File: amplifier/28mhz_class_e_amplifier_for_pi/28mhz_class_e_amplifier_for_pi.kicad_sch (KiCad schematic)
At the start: 20 parts, among them M1 RD16HHF1, U1 LT1818

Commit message: Switch to 50 ohm impedance
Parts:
- removed R5: 75, symbol ltspice:res
- added J1: Conn_Coaxial_Small, symbol Connector:Conn_Coaxial_Small
- added amp_matching1, matching_filter1, pre_main1: 0, symbol Device:R
- C10, C8: value 82p -> 130p; footprint Capacitor_SMD:C_0805_2012Metric -> (none)
- C7: value 130p -> 110p; footprint 0505:CAPC1514X130N -> (none)
- C9: value 150p -> 220p; footprint Capacitor_SMD:C_0805_2012Metric -> (none)
- L5: value 160n -> 140n; footprint Capacitor_SMD:C_0805_2012Metric -> (none)
- L6, L7: value 560n -> 390n; footprint 560nH:AISC-1008 -> (none)
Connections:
- net 0: now also J1.2 (Ext)
- net at C8.1, L6.2: now also matching_filter1.2; no longer C7.1
- net at R3.1, U1.3 (OUT): now also pre_main1.1; no longer M1.2 (G)
- net at L8.1, L9.1: now also amp_matching1.1; no longer C6.2
- net at C10.1, L7.1: now also J1.1 (In)
- new net: M1.2 (G), pre_main1.2
- new net: C6.2, amp_matching1.2
- new net: C7.1, matching_filter1.1

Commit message: current progress
footprints defined for everything except antenna and battery connectors
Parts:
- CF1: renamed from C8; value 130p -> 120p; footprint (none) -> Capacitor_SMD:C_0805_2012Metric
- CF2: renamed from C9; footprint (none) -> Capacitor_SMD:C_0805_2012Metric
- CF3: renamed from C10; value 130p -> 120p; footprint (none) -> Capacitor_SMD:C_0805_2012Metric
- CL1: renamed from C7; footprint (none) -> Capacitor_SMD:C_0805_2012Metric
- CS1: renamed from C6; value 190p -> 200p
- L2_a1: renamed from L8; value 1.8µ -> 1.5µ; footprint 1.8uH:LQH43MN470K03L -> Inductor_SMD:L_0805_2012Metric
- L2_b1: renamed from L9; value 470n -> 500n; footprint (none) -> wireinductor1:2929SQ501GEC
- LF1: renamed from L6; footprint (none) -> wireinductor0:2929SQ391GEC
- LF2: renamed from L7; footprint (none) -> wireinductor0:2929SQ391GEC
- LI1: renamed from L5; value 140n -> 130n; footprint (none) -> custom:130nH_WLQC2222H0GR13LB
- R0: renamed from pre_main1; footprint (none) -> Resistor_SMD:R_2512_6332Metric
- R1: renamed from amp_matching1; footprint (none) -> Resistor_SMD:R_2512_6332Metric
- R2: renamed from matching_filter1; footprint (none) -> Resistor_SMD:R_2512_6332Metric
- RF1: renamed from R3; footprint (none) -> 1Kohm:RESAD1625W54L665D240
- RI1: renamed from R1; footprint (none) -> 1Kohm:RESAD1625W54L665D240
- VBATTERY1: footprint (none) -> 1Kohm:RESAD1625W54L665D240
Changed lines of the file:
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@@
 		(on_board yes)
 		(dnp no)
-		(property "Reference" "C8"
+		(property "Reference" "CF1"
 			(at 231.775 109.855 0)
 			(effects
@@
 			)
 		)
-		(property "Value" "130p"
+		(property "Value" "120p"
 			(at 231.775 113.665 0)
 			(effects
@@
 			)
 		)
-		(property "Footprint" ""
+		(property "Footprint" "Capacitor_SMD:C_0805_2012Metric"
 			(at 229.87 109.22 0)
 			(effects
@@
 			(project ""
 				(path "/c76b4f53-cf38-425a-9e08-4e96ea8ec0d5"
-					(reference "C8")
+					(reference "CF1")
 					(unit 1)
 				)
@@
 		(on_board yes)
 		(dnp no)
-		(property "Reference" "L6"
+		(property "Reference" "LF1"
 			(at 236.855 103.2764 90)
 			(effects
@@
 			)
 		)
-		(property "Footprint" ""
+		(property "Footprint" "wireinductor0:2929SQ391GEC"
 			(at 241.3 102.87 0)
 			(effects
@@
 			(project ""
 				(path "/c76b4f53-cf38-425a-9e08-4e96ea8ec0d5"
-					(reference "L6")
+					(reference "LF1")
 					(unit 1)
 				)
@@
 		(on_board yes)
 		(dnp no)
-		(property "Reference" "R3"
+		(property "Reference" "RF1"
 			(at 88.1888 123.6726 90)
 			(effects
@@
 			)
 		)
-		(property "Footprint" ""
+		(property "Footprint" "1Kohm:RESAD1625W54L665D240"
 			(at 92.71 116.84 0)
 			(effects
@@
 			(project ""
 				(path "/c76b4f53-cf38-425a-9e08-4e96ea8ec0d5"
-					(reference "R3")
+					(reference "RF1")
 					(unit 1)
 				)
@@
 		(on_board yes)
 		(dnp no)
-		(property "Reference" "C6"
+		(property "Reference" "CS1"
 			(at 195.58 102.87 90)
 			(effects
@@
 			)
 		)
-		(property "Value" "190p"
+		(property "Value" "200p"
 			(at 195.58 105.41 90)
 			(effects
@@
 			(project ""
 				(path "/c76b4f53-cf38-425a-9e08-4e96ea8ec0d5"
-					(reference "C6")
+					(reference "CS1")
 					(unit 1)
 				)
@@
 		(on_board yes)
 		(dnp no)
-		(property "Reference" "L8"
+		(property "Reference" "L2_a1"
 			(at 161.925 99.4664 90)
 			(effects
@@
 			)
 		)
-		(property "Value" "1.8µ"
+		(property "Value" "1.5µ"
 			(at 161.925 101.6 90)
 			(effects
@@
 			)
 		)
-		(property "Footprint" "1.8uH:LQH43MN470K03L"
+		(property "Footprint" "Inductor_SMD:L_0805_2012Metric"
 			(at 166.37 99.06 0)
 			(effects
@@
 			(project ""
 				(path "/c76b4f53-cf38-425a-9e08-4e96ea8ec0d5"
-					(reference "L8")
+					(reference "L2_a1")
 					(unit 1)
 				)
@@
 		(on_board yes)
 		(dnp no)
-		(property "Reference" "C10"
+		(property "Reference" "CF3"
 			(at 262.255 109.855 0)
 			(effects
@@
 			)
 		)
-		(property "Value" "130p"
+		(property "Value" "120p"
 			(at 262.255 113.665 0)
 			(effects
@@
 			)
 		)
-		(property "Footprint" ""
+		(property "Footprint" "Capacitor_SMD:C_0805_2012Metric"
 			(at 260.35 109.22 0)
 			(effects
@@
 			(project ""
 				(path "/c76b4f53-cf38-425a-9e08-4e96ea8ec0d5"
-					(reference "C10")
+					(reference "CF3")
 					(unit 1)
 				)
@@
 			)
 		)
-		(property "Footprint" ""
+		(property "Footprint" "1Kohm:RESAD1625W54L665D240"
 			(at 106.68 93.98 0)
 			(effects
@@
 		(on_board yes)
 		(dnp no)
-		(property "Reference" "C7"
+		(property "Reference" "CL1"
 			(at 212.09 102.87 90)
 			(effects
@@
 			)
 		)
-		(property "Footprint" ""
+		(property "Footprint" "Capacitor_SMD:C_0805_2012Metric"
 			(at 214.63 102.87 0)
 			(effects
@@
 			(project ""
 				(path "/c76b4f53-cf38-425a-9e08-4e96ea8ec0d5"
-					(reference "C7")
+					(reference "CL1")
 					(unit 1)
 				)
@@
 		(on_board yes)
 		(dnp no)
-		(property "Reference" "L5"
+		(property "Reference" "LI1"
 			(at 204.8002 112.395 0)
 			(effects
@@
 			)
 		)
-		(property "Value" "140n"
+		(property "Value" "130n"
 			(at 204.8002 115.57 0)
 			(effects
@@
 			)
 		)
-		(property "Footprint" ""
+		(property "Footprint" "custom:130nH_WLQC2222H0GR13LB"
 			(at 201.93 109.22 0)
 			(effects
@@
 			(project ""
 				(path "/c76b4f53-cf38-425a-9e08-4e96ea8ec0d5"
-					(reference "L5")
+					(reference "LI1")
 					(unit 1)
 				)
@@
 		(on_board yes)
 		(dnp no)
-		(property "Reference" "L9"
+		(property "Reference" "L2_b1"
 			(at 161.925 107.0864 90)
 			(effects
@@
 			)
 		)
-		(property "Value" "470n"
+		(property "Value" "500n"
 			(at 161.925 109.22 90)
 			(effects
@@
 			)
 		)
-		(property "Footprint" ""
+		(property "Footprint" "wireinductor1:2929SQ501GEC"
 			(at 166.37 106.68 0)
 			(effects
@@
 			(project ""
 				(path "/c76b4f53-cf38-425a-9e08-4e96ea8ec0d5"
-					(reference "L9")
+					(reference "L2_b1")
 					(unit 1)
 				)
@@
 		(on_board yes)
 		(dnp no)
-		(property "Reference" "L7"
+		(property "Reference" "LF2"
 			(at 253.365 103.2764 90)
 			(effects
@@
 			)
 		)
-		(property "Footprint" ""
+		(property "Footprint" "wireinductor0:2929SQ391GEC"
 			(at 257.81 102.87 0)
 			(effects
@@
 			(project ""
 				(path "/c76b4f53-cf38-425a-9e08-4e96ea8ec0d5"
-					(reference "L7")
+					(reference "LF2")
 					(unit 1)
 				)
@@
 		(dnp no)
 		(fields_autoplaced yes)
-		(property "Reference" "amp_matching1"
+		(property "Reference" "R1"
 			(at 179.07 97.79 90)
 			(effects
@@
 			)
 		)
-		(property "Footprint" ""
+		(property "Footprint" "Resistor_SMD:R_2512_6332Metric"
 			(at 179.07 105.918 90)
 			(effects
@@
 			(project ""
 				(path "/c76b4f53-cf38-425a-9e08-4e96ea8ec0d5"
-					(reference "amp_matching1")
+					(reference "R1")
 					(unit 1)
 				)
@@
 		(on_board yes)
 		(dnp no)
-		(property "Reference" "R1"
+		(property "Reference" "RI1"
 			(at 77.8002 123.825 0)
 			(effects
@@
 			)
 		)
-		(property "Footprint" ""
+		(property "Footprint" "1Kohm:RESAD1625W54L665D240"
 			(at 74.93 120.65 0)
 			(effects
@@
 			(project ""
 				(path "/c76b4f53-cf38-425a-9e08-4e96ea8ec0d5"
-					(reference "R1")
+					(reference "RI1")
 					(unit 1)
 				)
@@
 				)
 				(justify bottom)
-				(hide yes)
 			)
 		)
@@
 				)
 				(justify top)
-				(hide yes)
 			)
 		)
@@
 		(dnp no)
 		(fields_autoplaced yes)
-		(property "Reference" "pre_main1"
+		(property "Reference" "R0"
 			(at 106.68 106.68 90)
 			(effects
@@
 			)
 		)
-		(property "Footprint" ""
+		(property "Footprint" "Resistor_SMD:R_2512_6332Metric"
 			(at 106.68 114.808 90)
 			(effects
@@
 			(project ""
 				(path "/c76b4f53-cf38-425a-9e08-4e96ea8ec0d5"
-					(reference "pre_main1")
+					(reference "R0")
 					(unit 1)
 				)
@@
 		(on_board yes)
 		(dnp no)
-		(property "Reference" "C9"
+		(property "Reference" "CF2"
 			(at 245.745 109.855 0)
 			(effects
@@
 			)
 		)
-		(property "Footprint" ""
+		(property "Footprint" "Capacitor_SMD:C_0805_2012Metric"
 			(at 243.84 109.22 0)
 			(effects
@@
 			(project ""
 				(path "/c76b4f53-cf38-425a-9e08-4e96ea8ec0d5"
-					(reference "C9")
+					(reference "CF2")
 					(unit 1)
 				)
@@
 		(dnp no)
 		(fields_autoplaced yes)
-		(property "Reference" "matching_filter1"
+		(property "Reference" "R2"
 			(at 223.52 97.79 90)
 			(effects
@@
 			)
 		)
-		(property "Footprint" ""
+		(property "Footprint" "Resistor_SMD:R_2512_6332Metric"
 			(at 223.52 105.918 90)
 			(effects
@@
 			(project "28mhz_class_e_amplifier_for_pi"
 				(path "/c76b4f53-cf38-425a-9e08-4e96ea8ec0d5"
-					(reference "matching_filter1")
-					(unit 1)
-				)
+					(reference "R2")
+					(unit 1)
+				)

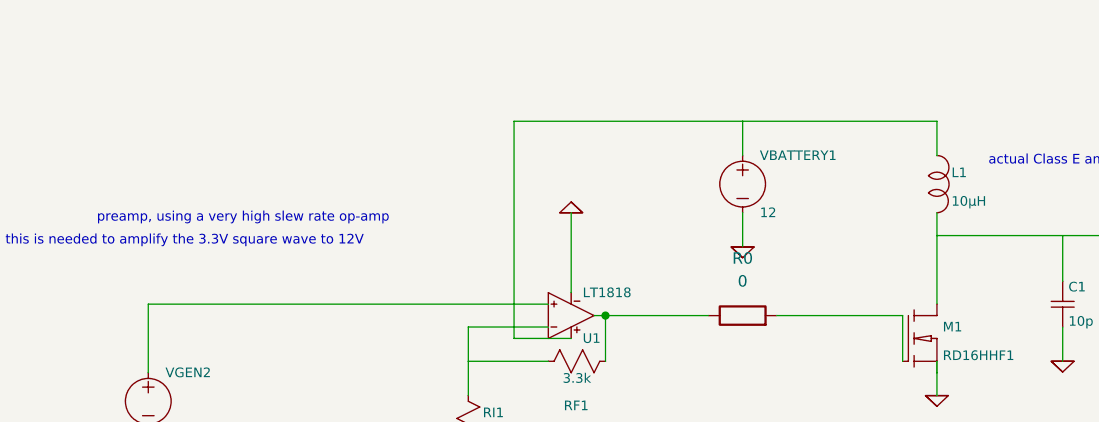
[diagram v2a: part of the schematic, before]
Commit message: ALL FOOTPRINTS ASSIGNED WE ARE COOKING
still need voltage regulator for Pi, it's ok :D
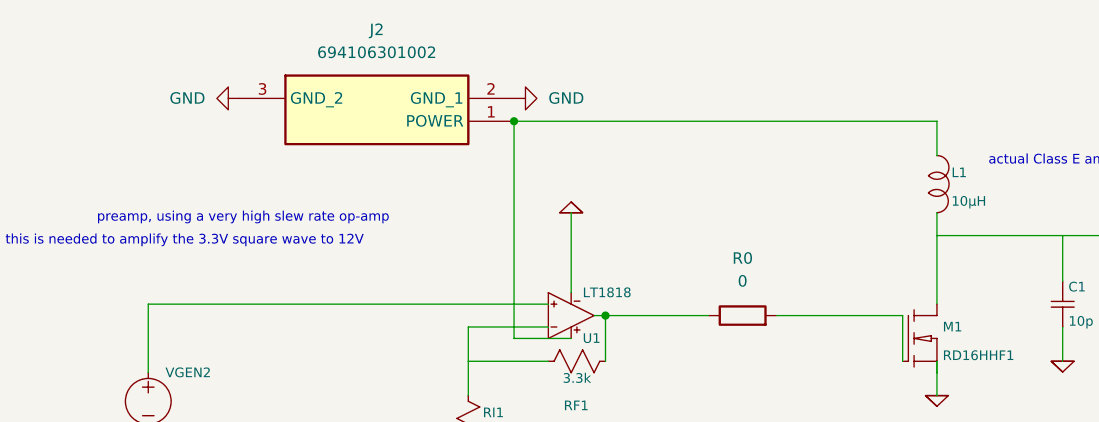
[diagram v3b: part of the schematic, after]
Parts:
- removed VBATTERY1: 12, 1Kohm:RESAD1625W54L665D240, symbol ltspice:voltage
- added J2: 694106301002, barreljack:694106301002_1, symbol barreljack:694106301002
- J1: footprint (none) -> BNC:CONBNC002
- VGEN2: footprint (none) -> Connector_PinHeader_2.54mm:PinHeader_1x02_P2.54mm_Vertical
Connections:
- net at L1.1, U1.4 (VCC): now also J2.1 (POWER)
- new net GND: J2.2 (GND_1), J2.3 (GND_2)
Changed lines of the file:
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@@
+		(color 0 0 0 0)
+	)
+	(junction
+		(at 81.28 91.44)
+		(diameter 0)
 		(color 0 0 0 0)
 	)
@@
 	(wire
 		(pts
-			(xy 106.68 105.41) (xy 106.68 101.6)
-		)
-		(stroke
-			(width 0.1524)
-			(type solid)
-		)
-	)
-	(wire
-		(pts
 			(xy 214.63 104.14) (xy 219.71 104.14)
 		)
@@
 	(wire
 		(pts
-			(xy 106.68 95.25) (xy 106.68 91.44)
-		)
-		(stroke
-			(width 0.1524)
-			(type solid)
-		)
-	)
-	(wire
-		(pts
 			(xy 245.11 109.22) (xy 245.11 104.14)
 		)
@@
 	(wire
 		(pts
-			(xy 128.27 91.44) (xy 106.68 91.44)
-		)
-		(stroke
-			(width 0.1524)
-			(type solid)
-		)
-	)
-	(wire
-		(pts
 			(xy 142.24 109.22) (xy 142.24 104.14)
 		)
@@
 	(wire
 		(pts
-			(xy 106.68 91.44) (xy 81.28 91.44)
+			(xy 81.28 91.44) (xy 128.27 91.44)
 		)
 		(stroke
@@
 				(path "/c76b4f53-cf38-425a-9e08-4e96ea8ec0d5"
 					(reference "CF3")
-					(unit 1)
-				)
-			)
-		)
-	)
-	(symbol
-		(lib_id "ltspice:voltage")
-		(at 106.68 93.98 0)
-		(unit 1)
-		(exclude_from_sim no)
-		(in_bom yes)
-		(on_board yes)
-		(dnp no)
-		(property "Reference" "VBATTERY1"
-			(at 108.585 95.25 0)
-			(effects
-				(font
-					(size 1.0668 1.0668)
-				)
-				(justify left)
-			)
-		)
-		(property "Value" "12"
-			(at 108.585 101.6 0)
-			(effects
-				(font
-					(size 1.0668 1.0668)
-				)
-				(justify left)
-			)
-		)
-		(property "Footprint" "1Kohm:RESAD1625W54L665D240"
-			(at 106.68 93.98 0)
-			(effects
-				(font
-					(size 1.27 1.27)
-				)
-				(hide yes)
-			)
-		)
-		(property "Datasheet" ""
-			(at 106.68 93.98 0)
-			(effects
-				(font
-					(size 1.27 1.27)
-				)
-				(hide yes)
-			)
-		)
-		(property "Description" ""
-			(at 106.68 93.98 0)
-			(effects
-				(font
-					(size 1.27 1.27)
-				)
-				(hide yes)
-			)
-		)
-		(property "Sim.Device" "SPICE"
-			(at 106.68 93.98 0)
-			(effects
-				(font
-					(size 1.27 1.27)
-				)
-				(hide yes)
-			)
-		)
-		(property "Sim.Params" "type=\"V\" model=\"${VALUE}\" "
-			(at 106.68 93.98 0)
-			(effects
-				(font
-					(size 1.0668 1.0668)
-				)
-				(justify left)
-				(hide yes)
-			)
-		)
-		(pin "1"
-		)
-		(pin "2"
-		)
-		(instances
-			(project ""
-				(path "/c76b4f53-cf38-425a-9e08-4e96ea8ec0d5"
-					(reference "VBATTERY1")
 					(unit 1)
 				)
@@
 			)
 		)
-		(property "Footprint" ""
+		(property "Footprint" "BNC:CONBNC002"
 			(at 273.05 110.49 0)
 			(effects
@@
 			)
 		)
-		(property "Footprint" ""
+		(property "Footprint" "Connector_PinHeader_2.54mm:PinHeader_1x02_P2.54mm_Vertical"
 			(at 40.64 118.11 0)
 			(effects
@@
 	)
 	(symbol
+		(lib_id "barreljack:694106301002")
+		(at 50.8 88.9 0)
+		(unit 1)
+		(exclude_from_sim no)
+		(in_bom yes)
+		(on_board yes)
+		(dnp no)
+		(fields_autoplaced yes)
+		(property "Reference" "J2"
+			(at 66.04 81.28 0)
+			(effects
+				(font
+					(size 1.27 1.27)
+				)
+			)
+		)
+		(property "Value" "694106301002"
+			(at 66.04 83.82 0)
+			(effects
+				(font
+					(size 1.27 1.27)
+				)
+			)
+		)
+		(property "Footprint" "barreljack:694106301002_1"
+			(at 77.47 183.82 0)
+			(effects
+				(font
+					(size 1.27 1.27)
+				)
+				(justify left top)
+				(hide yes)
+			)
+		)
+		(property "Datasheet" "https://datasheet.datasheetarchive.com/originals/distributors/Datasheets_SAMA/1c153bd2ba42bb51bda59ee4cd9765cd.pdf"
+			(at 77.47 283.82 0)
+			(effects
+				(font
+					(size 1.27 1.27)
+				)
+				(justify left top)
+				(hide yes)
+			)
+		)
+		(property "Description" "WURTH ELEKTRONIK - 694106301002 - CONNECTOR, POWER ENTRY, JACK, 3A, 20VDC"
+			(at 50.8 88.9 0)
+			(effects
+				(font
+					(size 1.27 1.27)
+				)
+				(hide yes)
+			)
+		)
+		(property "Height" ""
+			(at 77.47 483.82 0)
+			(effects
+				(font
+					(size 1.27 1.27)
+				)
+				(justify left top)
+				(hide yes)
+			)
+		)
+		(property "Mouser Part Number" "710-694106301002"
+			(at 77.47 583.82 0)
+			(effects
+				(font
+					(size 1.27 1.27)
+				)
+				(justify left top)
+				(hide yes)
+			)
+		)
+		(property "Mouser Price/Stock" "https://www.mouser.co.uk/ProductDetail/Wurth-Elektronik/694106301002?qs=a9WhcLg8qCwOEkcI62k5mA%3D%3D"
+			(at 77.47 683.82 0)
+			(effects
+				(font
+					(size 1.27 1.27)
+				)
+				(justify left top)
+				(hide yes)
+			)
+		)
+		(property "Manufacturer_Name" "Wurth Elektronik"
+			(at 77.47 783.82 0)
+			(effects
+				(font
+					(size 1.27 1.27)
+				)
+				(justify left top)
+				(hide yes)
+			)
+		)
+		(property "Manufacturer_Part_Number" "694106301002"
+			(at 77.47 883.82 0)
+			(effects
+				(font
+					(size 1.27 1.27)
+				)
+				(justify left top)
+				(hide yes)
+			)
+		)
+		(pin "3"
+		)
+		(pin "2"
+		)
+		(pin "1"
+		)
+		(instances
+			(project ""
+				(path "/c76b4f53-cf38-425a-9e08-4e96ea8ec0d5"
+					(reference "J2")
+					(unit 1)
+				)
+			)
+		)
+	)
+	(symbol
 		(lib_id "ltspice:cap")
 		(at 153.67 102.87 270)
@@
 				(path "/c76b4f53-cf38-425a-9e08-4e96ea8ec0d5"
 					(reference "#GND03")
+					(unit 1)
+				)
+			)
+		)
+	)
+	(symbol
+		(lib_id "power:GND")
+		(at 81.28 88.9 90)
+		(unit 1)
+		(exclude_from_sim no)
+		(in_bom yes)
+		(on_board yes)
+		(dnp no)
+		(fields_autoplaced yes)
+		(property "Reference" "#PWR01"
+			(at 87.63 88.9 0)
+			(effects
+				(font
+					(size 1.27 1.27)
+				)
+				(hide yes)
+			)
+		)
+		(property "Value" "GND"
+			(at 85.09 88.8999 90)
+			(effects
+				(font
+					(size 1.27 1.27)
+				)
+				(justify right)
+			)
+		)
+		(property "Footprint" ""
+			(at 81.28 88.9 0)
+			(effects
+				(font
+					(size 1.27 1.27)
+				)
+				(hide yes)
+			)
+		)
+		(property "Datasheet" ""
+			(at 81.28 88.9 0)
+			(effects
+				(font
+					(size 1.27 1.27)
+				)
+				(hide yes)
+			)
+		)
+		(property "Description" "Power symbol creates a global label with name \"GND\" , ground"
+			(at 81.28 88.9 0)
+			(effects
+				(font
+					(size 1.27 1.27)
+				)
+				(hide yes)
+			)
+		)
+		(pin "1"
+		)
+		(instances
+			(project ""
+				(path "/c76b4f53-cf38-425a-9e08-4e96ea8ec0d5"
+					(reference "#PWR01")
 					(unit 1)
 				)
@@
 	)
 	(symbol
-		(lib_id "ltspice:GND")
-		(at 106.68 105.41 0)
+		(lib_id "power:GND")
+		(at 50.8 88.9 270)
 		(unit 1)
 		(exclude_from_sim no)
@@
 		(on_board yes)
 		(dnp no)
-		(property "Reference" "#GND01"
-			(at 106.68 105.41 0)
-			(effects
-				(font
-					(size 1.27 1.27)
-				)
-				(hide yes)
-			)
-		)
-		(property "Value" "0"
-			(at 106.68 105.41 0)
-			(effects
-				(font
-					(size 1.0668 1.0668)
-				)
-				(hide yes)
+		(fields_autoplaced yes)
+		(property "Reference" "#PWR02"
+			(at 44.45 88.9 0)
+			(effects
+				(font
+					(size 1.27 1.27)
+				)
+				(hide yes)
+			)
+		)
+		(property "Value" "GND"
+			(at 46.99 88.8999 90)
+			(effects
+				(font
+					(size 1.27 1.27)
+				)
+				(justify right)
 			)
 		)
 		(property "Footprint" ""
-			(at 106.68 105.41 0)
+			(at 50.8 88.9 0)
 			(effects
 				(font
@@
 		)
 		(property "Datasheet" ""
-			(at 106.68 105.41 0)
-			(effects
-				(font
-					(size 1.27 1.27)
-				)
-				(hide yes)
-			)
-		)
-		(property "Description" ""
-			(at 106.68 105.41 0)
-			(effects
-				(font
-					(size 1.27 1.27)
-				)
-				(hide yes)
-			)
-		)
-		(pin ""
+			(at 50.8 88.9 0)
+			(effects
+				(font
+					(size 1.27 1.27)
+				)
+				(hide yes)
+			)
+		)
+		(property "Description" "Power symbol creates a global label with name \"GND\" , ground"
+			(at 50.8 88.9 0)
+			(effects
+				(font
+					(size 1.27 1.27)
+				)
+				(hide yes)
+			)
+		)
+		(pin "1"
 		)
 		(instances
-			(project ""
+			(project "28mhz_class_e_amplifier_for_pi"
 				(path "/c76b4f53-cf38-425a-9e08-4e96ea8ec0d5"
-					(reference "#GND01")
+					(reference "#PWR02")
 					(unit 1)
 				)

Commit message: Everything except routing done
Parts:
- removed VGEN2: PULSE(0 3.3 0 1n 1n {0.5/freq} {1/freq}), Connector_PinHeader_2.54mm:PinHeader_1x02_P2.54mm_Vertical, symbol ltspice:voltage
- added C3: 0.1u, Capacitor_SMD:C_0805_2012Metric, symbol Device:C
- added C4: 0.33u, Capacitor_SMD:C_0805_2012Metric, symbol Device:C
- added J3: Conn_01x03_Socket, Connector_PinSocket_2.54mm:PinSocket_1x03_P2.54mm_Vertical, symbol Connector:Conn_01x03_Socket
- added U2: LM7805_TO220, Package_TO_SOT_THT:TO-220-3_Vertical, symbol Regulator_Linear:LM7805_TO220
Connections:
- net GND: now also C3.2, C4.2, J3.3 (Pin_3), U2.2 (GND)
- net at U1.1 (IN+): now also J3.2 (Pin_2)
- new net: C3.1, J3.1 (Pin_1), U2.3 (VO)
- new net: C4.1, U2.1 (VI)
